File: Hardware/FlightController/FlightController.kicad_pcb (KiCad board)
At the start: 4 copper layers, 54 x 52 mm, 59 parts, among them J1 Conn_01x02, J10 Conn_01x03, J11 Conn_01x04, J12 Conn_01x03, J13 Conn_01x02, J2 USB_B_Mini, J3 Conn_02x03_Odd_Even, J4 Conn_01x04, J5 Conn_01x03, J6 Conn_01x03, J7 Conn_01x03, J8 Conn_01x03, J9 Conn_01x03, Q1 MMBT3904, SW1 SW_SPDT, SW2 SW_SPDT, U1 STM32F405RGT6, U2 MPU-6050, U3 TPS54331DR, U4 USBLC6-2SC6, Y1 16MHz

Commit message: Update footprints, routing and LCSC numbers
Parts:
- removed the C18 at (158.7, 120.3)
- removed F1: 750mA, Fuse:Fuse_0402_1005Metric
- added D2: LED, LED_SMD:LED_0603_1608Metric, F.Cu at (162.9, 117.8)
- added H4: MountingHole_Pad, MountingHole:MountingHole_2.5mm_Pad, F.Cu at (117.5, 122.5)
- added R12: 10k, Resistor_SMD:R_0603_1608Metric, F.Cu at (163.7, 120.5)
- added U3: W25Q128JVS, Package_SO:SOIC-8_5.23x5.23mm_P1.27mm, F.Cu at (133.8, 85.9)
- C11: renamed from C21; footprint Capacitor_SMD:C_0402_1005Metric -> Capacitor_SMD:C_0603_1608Metric_Pad1.08x0.95mm_HandSolder
- C12: renamed from C22; footprint Capacitor_SMD:C_0402_1005Metric -> Capacitor_SMD:C_0603_1608Metric_Pad1.08x0.95mm_HandSolder
- C13: renamed from C23; footprint Capacitor_SMD:C_0402_1005Metric -> Capacitor_SMD:C_0603_1608Metric_Pad1.08x0.95mm_HandSolder
- C15: renamed from C1; footprint Capacitor_SMD:C_0402_1005Metric -> Capacitor_SMD:C_0603_1608Metric
- C16: renamed from C2; footprint Capacitor_SMD:C_0402_1005Metric -> Capacitor_SMD:C_0603_1608Metric
- C17: renamed from C3; value 3nF -> 1nF; footprint Capacitor_SMD:C_0402_1005Metric -> Capacitor_SMD:C_0603_1608Metric
- C18: renamed from C4; footprint Capacitor_SMD:C_0402_1005Metric -> Capacitor_SMD:C_0603_1608Metric
- C19: renamed from C5; footprint Capacitor_SMD:C_0402_1005Metric -> Capacitor_SMD:C_0603_1608Metric
- C20: renamed from C15; value 22uF -> 100uF; footprint Capacitor_SMD:C_0402_1005Metric -> Capacitor_SMD:C_1206_3216Metric
- C5: renamed from C8; footprint Capacitor_SMD:C_0402_1005Metric -> Capacitor_SMD:C_0603_1608Metric
- D1: value PMEG4010EJ -> SS14; footprint Diode_SMD:D_SOD-323F -> Diode_SMD:D_SMA
- L1: value 6.8uH -> 3.3uH; footprint Inductor_SMD:L_0402_1005Metric -> Inductor_SMD:L_1008_2520Metric_Pad1.43x2.20mm_HandSolder
- R1: renamed from R10; footprint Resistor_SMD:R_0402_1005Metric -> Resistor_SMD:R_0603_1608Metric
- R10: renamed from R2; footprint Resistor_SMD:R_0402_1005Metric -> Resistor_SMD:R_0805_2012Metric_Pad1.20x1.40mm_HandSolder
- R11: renamed from R7; footprint Resistor_SMD:R_0402_1005Metric -> Resistor_SMD:R_0603_1608Metric_Pad0.98x0.95mm_HandSolder
- R2: renamed from R11; footprint Resistor_SMD:R_0402_1005Metric -> Resistor_SMD:R_0603_1608Metric
- R3: footprint Resistor_SMD:R_0402_1005Metric -> Resistor_SMD:R_0603_1608Metric
- R9: renamed from R1; value 11.5k -> 41.2k; footprint Resistor_SMD:R_0402_1005Metric -> Resistor_SMD:R_0603_1608Metric_Pad0.98x0.95mm_HandSolder
- moved H2 44.6 mm to (117.5, 77.5)
- moved R3 8.16 mm to (136.2, 81.7)
- moved SW1 7.00 mm to (125.0, 84.0), turned to 90 degrees
- moved H1 4.03 mm to (170.0, 122.5)
- moved H3 4.03 mm to (170.0, 77.5)
- moved L1 3.67 mm to (162.1, 114.6)
- moved J2 3.45 mm to (168.4, 96.9)
- moved J13 3.38 mm to (166.9, 111.2)
- moved C20 2.53 mm to (160.0, 120.6)
- moved C17 1.70 mm to (159.0, 116.3)
- moved D1 1.58 mm to (155.2, 112.8)
- moved R9 1.10 mm to (156.2, 115.5)
- moved R10 1.07 mm to (156.3, 121.6)
- moved C11 0.94 mm to (147.3, 79.4)
- moved C12 0.94 mm to (141.8, 83.0), turned to 90 degrees
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- renumbered C6 to C1, C16 to C10, C24 to C14, C7 to C2, C10 to C3, C12 to C4, C9 to C6, C11 to C7, C13 to C8, C14 to C9, J12 to J1, J13 to J12, J1 to J13, R8 to R7, R9 to R8, U4 to U2, U2 to U4, U3 to U5
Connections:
- net /MCU/SBUS_RX_INV renamed Net-(J1-Pad1)
- C20 pad 1: Net-(C15-Pad1) -> +3V3
- L1 pad 2: Net-(C15-Pad1) -> +3V3
- R10 pad 1: Net-(C15-Pad1) -> +3V3
- U1 pad 61: unconnected-(U1-Pad61) -> S_SPI1_CS
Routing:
- net GND: track 55.9 -> 83.3 mm, vias 93 -> 42
- net S_SPI1_SCK: track 0.00 -> 23.3 mm, vias 0 -> 2
- net S_SPI1_MOSI: track 0.00 -> 18.2 mm, vias 0 -> 2
- net S_SPI1_MISO: track 0.00 -> 12.8 mm, vias 0 -> 2
- net +3V3: track 35.1 -> 47.3 mm, vias 12 -> 13
- net S_BOOT0: track 3.98 -> 13.4 mm
- net Net-(C15-Pad1): track 8.60 -> 0.00 mm
- net Net-(C19-Pad2): track 11.2 -> 18.3 mm
- net S_SPI1_CS: track 0.00 -> 6.82 mm
- net USB_5v: track 16.5 -> 20.5 mm
- net USB_CONN_DM: track 5.27 -> 8.72 mm
- net USB_CONN_DP: track 5.69 -> 9.05 mm
- net PDB_REG_5v: track 11.8 -> 9.39 mm
- net +5V: track 43.5 -> 41.5 mm, vias 2 -> 1
- net Net-(D2-Pad1): track 0.00 -> 1.88 mm
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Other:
- board size 54 x 52 mm -> 62.5 x 55 mm
- board text added: "CLK"
- board text added: "DIO"
- board text added: "GND"
- board text added: "RST"
- board text added: "SWO"
- board text added: "TX"
- board text added: "Tejas Maraliga"
- board text removed: "HIGH"
- board text removed: "LOW"

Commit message: Finalize design and routing for v1.0 fab
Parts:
- J2: value USB_B_Mini -> 690-005-299-043; footprint digikey-footprints:USB_Mini_B_Female_UX60-MB-5ST -> digikey-footprints:USB_Mini_B_Female_690-005-299-043
- moved J2 0.38 mm to (168.8, 96.8), turned to 180 degrees
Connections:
- net S_USB_DM renamed S_USB_D-
- net S_USB_DP renamed S_USB_D+
- net USB_CONN_DM renamed USB_CONN_D-
- net USB_CONN_DP renamed USB_CONN_D+
- J2 pad SH: (no net) -> unconnected-(J2-PadSH)
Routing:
- net unconnected-(J2-PadSH): track 0.00 -> 19.9 mm
- net S_SWO: track 22.5 -> 23.5 mm
- net USB_CONN_D-: track 8.72 -> 9.39 mm
- net SBUS_TX: track 24.0 -> 24.7 mm
- net S_SBUS_RX: track 20.7 -> 21.3 mm
- net S_I2C2_SCL: track 32.2 -> 32.6 mm, vias 2 -> 1
- net GND: track 83.3 -> 82.9 mm, vias 42 -> 30
- net S_I2C2_SDA: track 33.8 -> 33.5 mm, vias 2 -> 1
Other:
- board text added: "-> +X"
- board text added: "-> +Y"
- board text added: "JLCJLCJLCJLC"

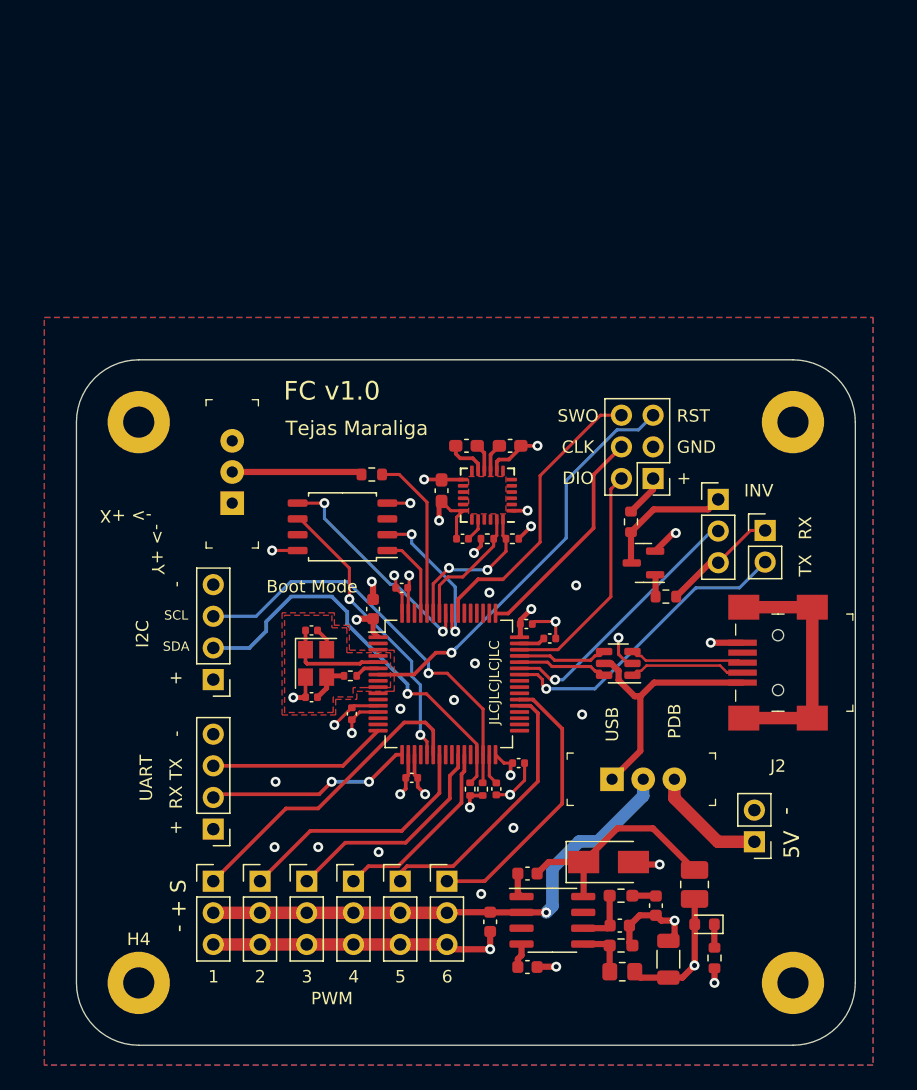
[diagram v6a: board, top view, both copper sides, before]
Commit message: Read and stream acceleration values from MPU6050
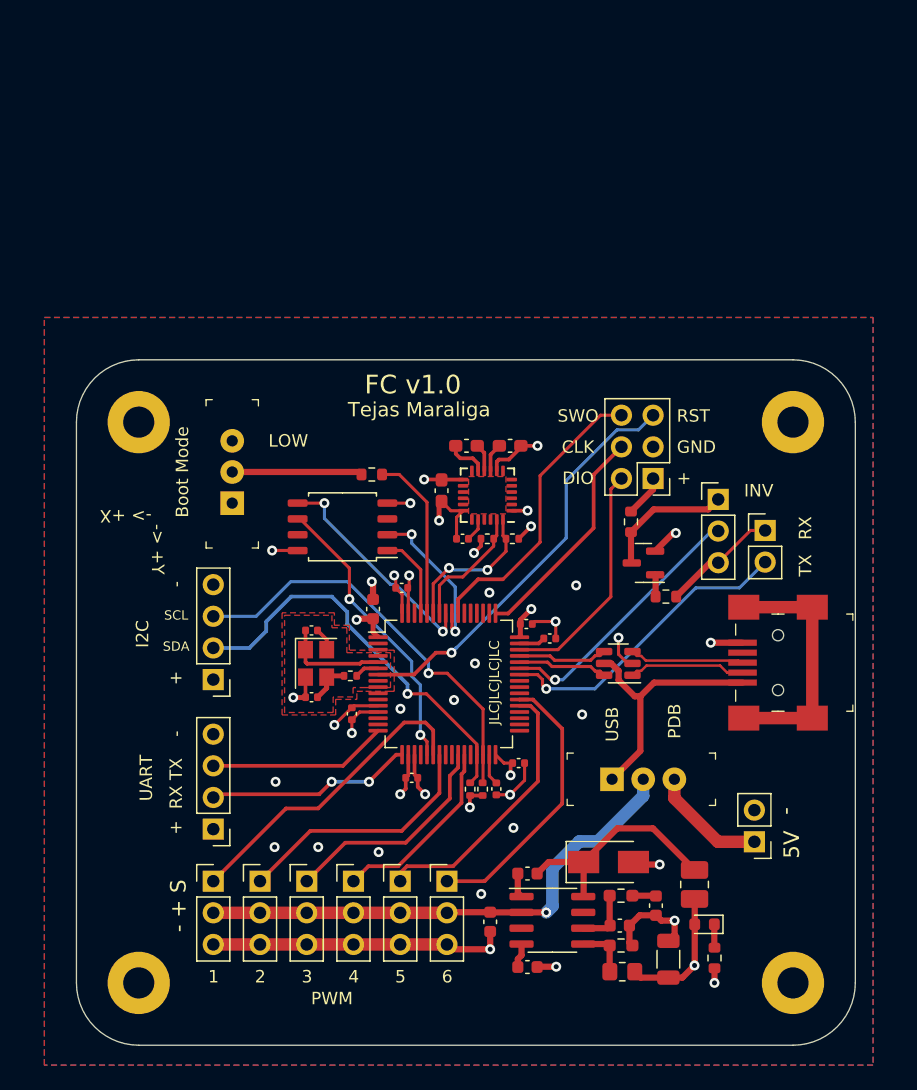
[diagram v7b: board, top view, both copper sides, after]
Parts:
- renumbered J2 to Je
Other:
- board text added: "LOW"
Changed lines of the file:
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@@
     (property "Status" "Active")
     (attr smd)
-    (fp_text reference "J2" (at 0 -8.3) (layer "F.SilkS")
+    (fp_text reference "Je" (at 0 -8.3) (layer "F.SilkS") hide
       (effects (font (size 1 1) (thickness 0.15)))
     )
@@
     (property "Sheetname" "Connectors")
     (attr exclude_from_pos_files)
-    (fp_text reference "H4" (at 0 -3.5) (layer "F.SilkS")
+    (fp_text reference "H4" (at 0 -3.5) (layer "F.SilkS") hide
       (effects (font (size 1 1) (thickness 0.15)))
     )
@@
     (effects (font (size 1 1) (thickness 0.15)))
   )
-  (gr_text "FC v1.0" (at 133 75) (layer "F.SilkS")
+  (gr_text "FC v1.0" (at 139.5 74.5) (layer "F.SilkS")
     (effects (font (size 1.5 1.5) (thickness 0.25)))
   )
@@
     (effects (font (size 1 1) (thickness 0.15)))
   )
-  (gr_text "Tejas Maraliga" (at 135 78) (layer "F.SilkS")
+  (gr_text "Tejas Maraliga" (at 140 76.5) (layer "F.SilkS")
     (effects (font (size 1.15 1.15) (thickness 0.25)))
   )
@@
     (effects (font (size 1 1) (thickness 0.15)))
   )
-  (gr_text "Boot Mode" (at 131.4 90.7) (layer "F.SilkS")
+  (gr_text "Boot Mode" (at 121 81.5 90) (layer "F.SilkS")
     (effects (font (size 1 1) (thickness 0.15)))
   )
@@
     (effects (font (size 1 1) (thickness 0.15)))
   )
+  (gr_text "LOW" (at 129.5 79) (layer "F.SilkS")
+    (effects (font (size 1 1) (thickness 0.15)))
+  )
